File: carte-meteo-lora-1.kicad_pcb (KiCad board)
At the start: 2 copper layers, 60 x 45 mm, 121 parts, among them J1 TC2030, J2 Conn_01x04, J3 Conn_01x04, J4 Conn_Coaxial, J5 USB_C_Receptacle_USB2.0_14P, J6 Solar_Cell, J7 Conn_01x02, J8 Battery_Cell, Q1 AO4882, Q2 AO4882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

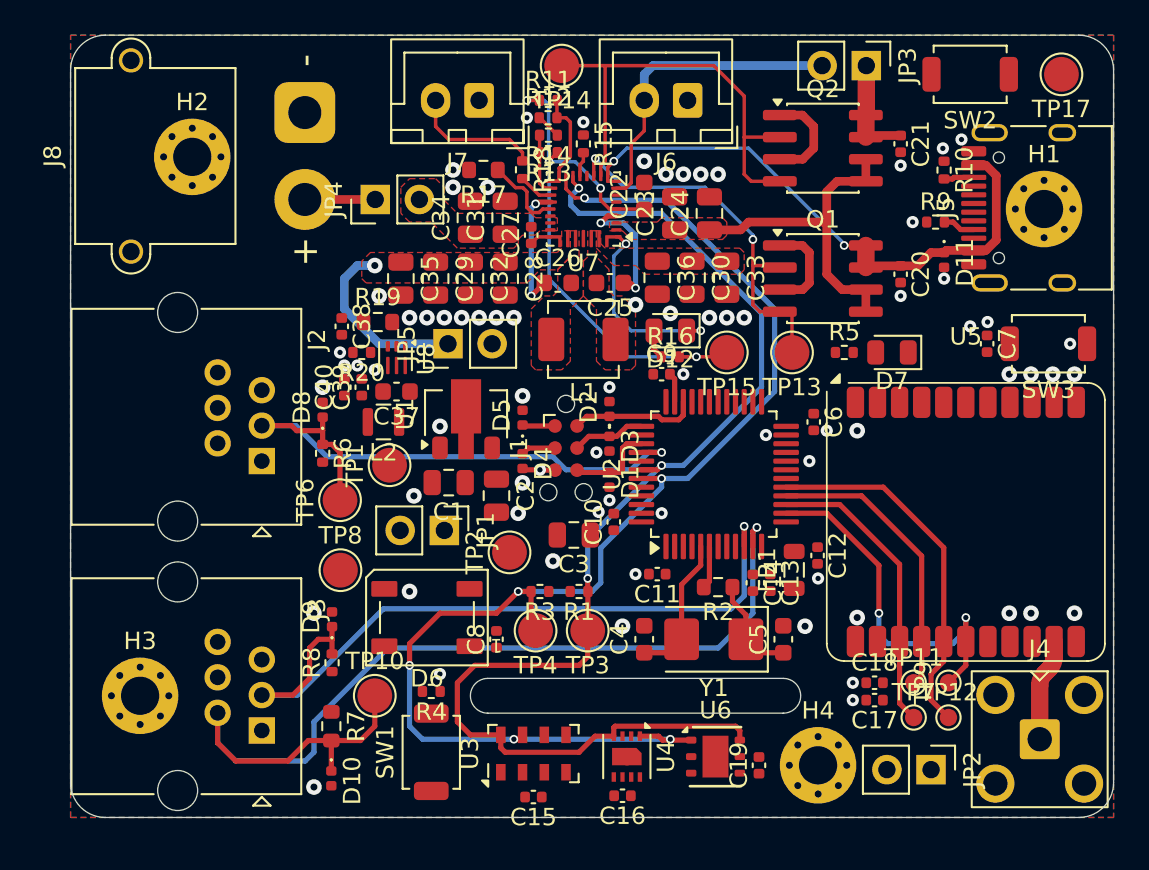
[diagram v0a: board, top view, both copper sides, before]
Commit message: pcb: add smps and +5v pwr routing
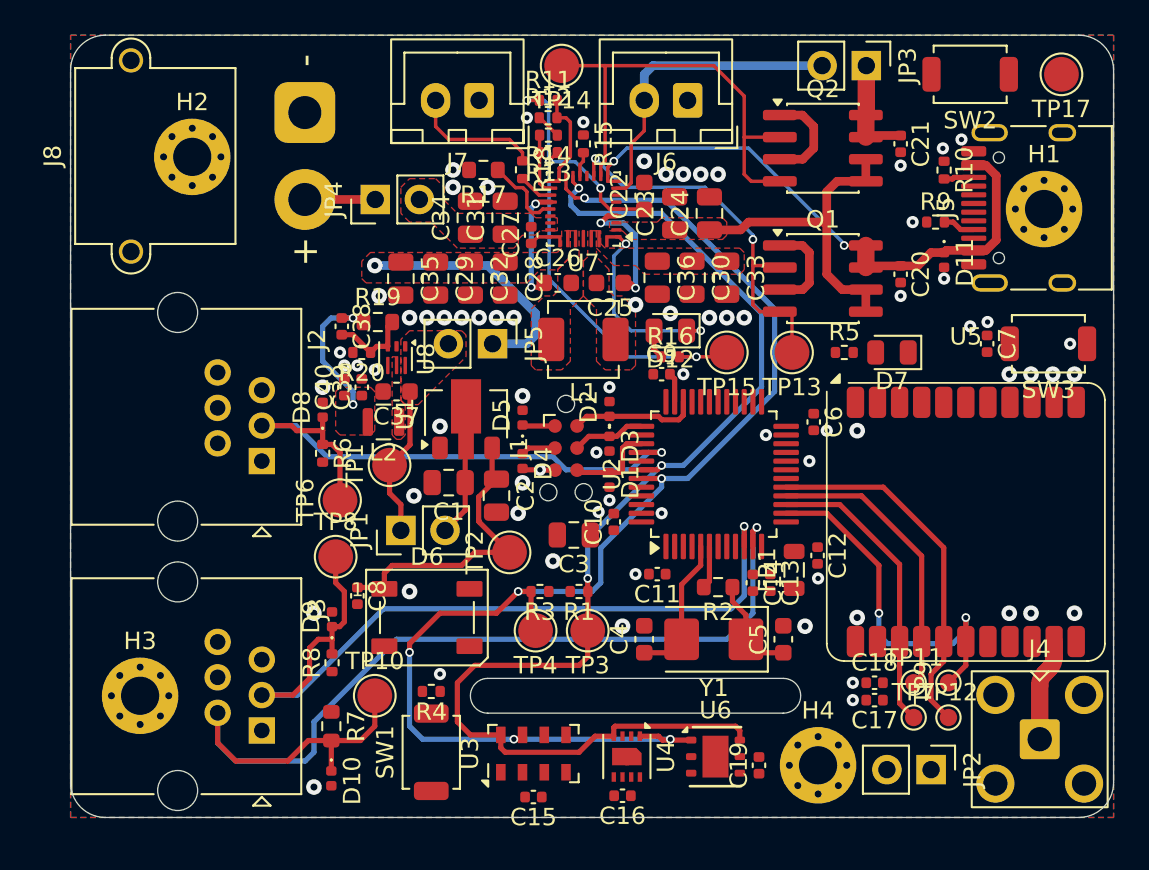
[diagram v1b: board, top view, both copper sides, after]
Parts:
- moved C8 8.38 mm to (66.5, 55.2), turned to -90 degrees
- moved JP5 2.57 mm to (74.3, 40.8), turned to -90 degrees
- moved JP1 2.50 mm to (69.0, 51.5), turned to 90 degrees
- moved TP8 0.82 mm to (65.2, 53.0)
- turned D6 to 0 degrees
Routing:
- net +SYS: track 10.6 -> 28.4 mm
- net +5V: track 0.00 -> 17.5 mm
- net +3V3: track 1.89 -> 10.4 mm, vias 0 -> 2
- net /WIND: track 43.2 -> 48.0 mm
- net Net-(U8-FB): track 0.00 -> 4.72 mm
- net Net-(U7-BTST2): track 7.39 -> 6.69 mm
- added copper zone on F.Cu, net +3V3
- added copper zone on F.Cu, net Net-(U8-SW)

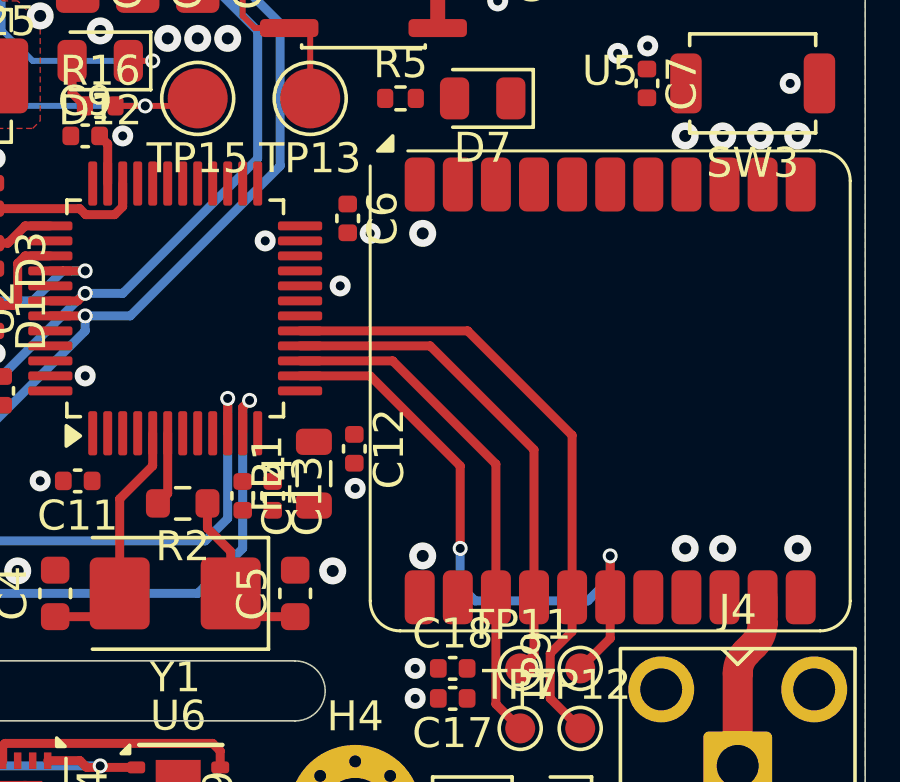
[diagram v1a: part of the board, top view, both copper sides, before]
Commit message: pcb: add lora gpio routing
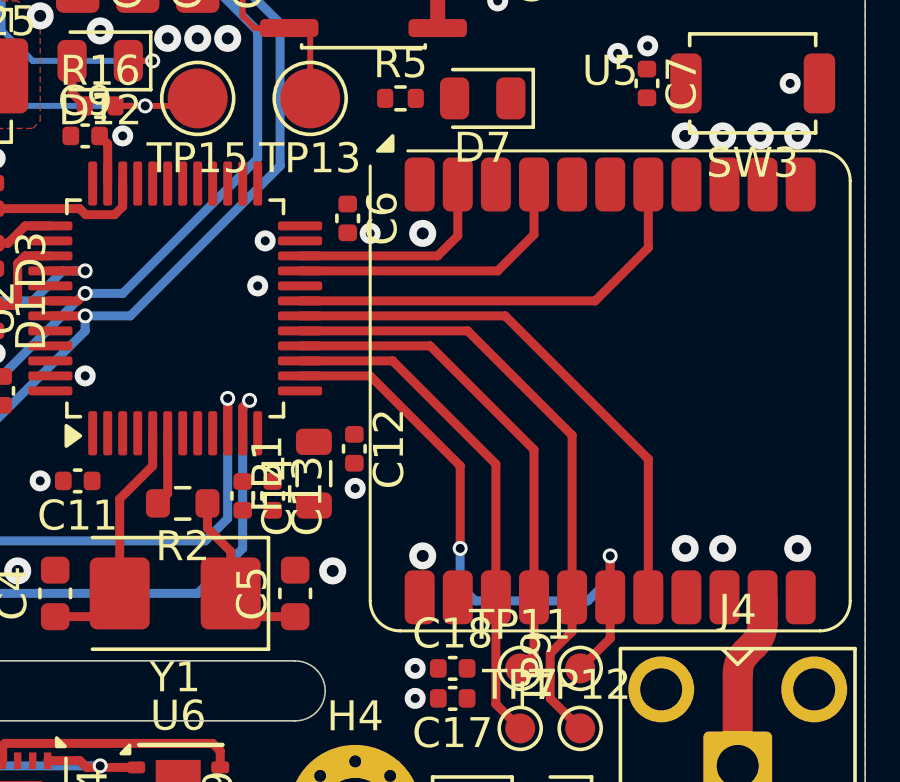
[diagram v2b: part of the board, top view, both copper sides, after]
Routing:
- net /RST: track 0.00 -> 18.2 mm
- net /DIO1: track 0.00 -> 14.5 mm
- net /DIO3: track 0.00 -> 9.97 mm
- net /BUSY: track 0.00 -> 7.25 mm
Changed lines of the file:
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@@
 	)
 	(via
-		(at 92.5 47.5)
+		(at 89.75 47.5)
 		(size 0.7)
 		(drill 0.3)
@@
 	)
 	(segment
+		(start 98 48.5)
+		(end 102.77 53.27)
+		(width 0.3)
+		(layer "F.Cu")
+		(net "/RST")
+	)
+	(segment
+		(start 91.1625 48.5)
+		(end 98 48.5)
+		(width 0.3)
+		(layer "F.Cu")
+		(net "/RST")
+	)
+	(segment
+		(start 102.77 53.27)
+		(end 102.77 57.88)
+		(width 0.3)
+		(layer "F.Cu")
+		(net "/RST")
+	)
+	(segment
+		(start 98.96 45.79)
+		(end 98.96 44.12)
+		(width 0.3)
+		(layer "F.Cu")
+		(net "/DIO3")
+	)
+	(segment
+		(start 97.75 47)
+		(end 98.96 45.79)
+		(width 0.3)
+		(layer "F.Cu")
+		(net "/DIO3")
+	)
+	(segment
+		(start 91.1625 47)
+		(end 97.75 47)
+		(width 0.3)
+		(layer "F.Cu")
+		(net "/DIO3")
+	)
+	(segment
+		(start 101 48)
+		(end 102.77 46.23)
+		(width 0.3)
+		(layer "F.Cu")
+		(net "/DIO1")
+	)
+	(segment
+		(start 91.1625 48)
+		(end 101 48)
+		(width 0.3)
+		(layer "F.Cu")
+		(net "/DIO1")
+	)
+	(segment
+		(start 102.77 46.23)
+		(end 102.77 44.12)
+		(width 0.3)
+		(layer "F.Cu")
+		(net "/DIO1")
+	)
+	(segment
+		(start 91.1625 46.5)
+		(end 95.75 46.5)
+		(width 0.3)
+		(layer "F.Cu")
+		(net "/BUSY")
+	)
+	(segment
+		(start 96.42 45.83)
+		(end 96.42 44.12)
+		(width 0.3)
+		(layer "F.Cu")
+		(net "/BUSY")
+	)
+	(segment
+		(start 95.75 46.5)
+		(end 96.42 45.83)
+		(width 0.3)
+		(layer "F.Cu")
+		(net "/BUSY")
+	)
+	(segment

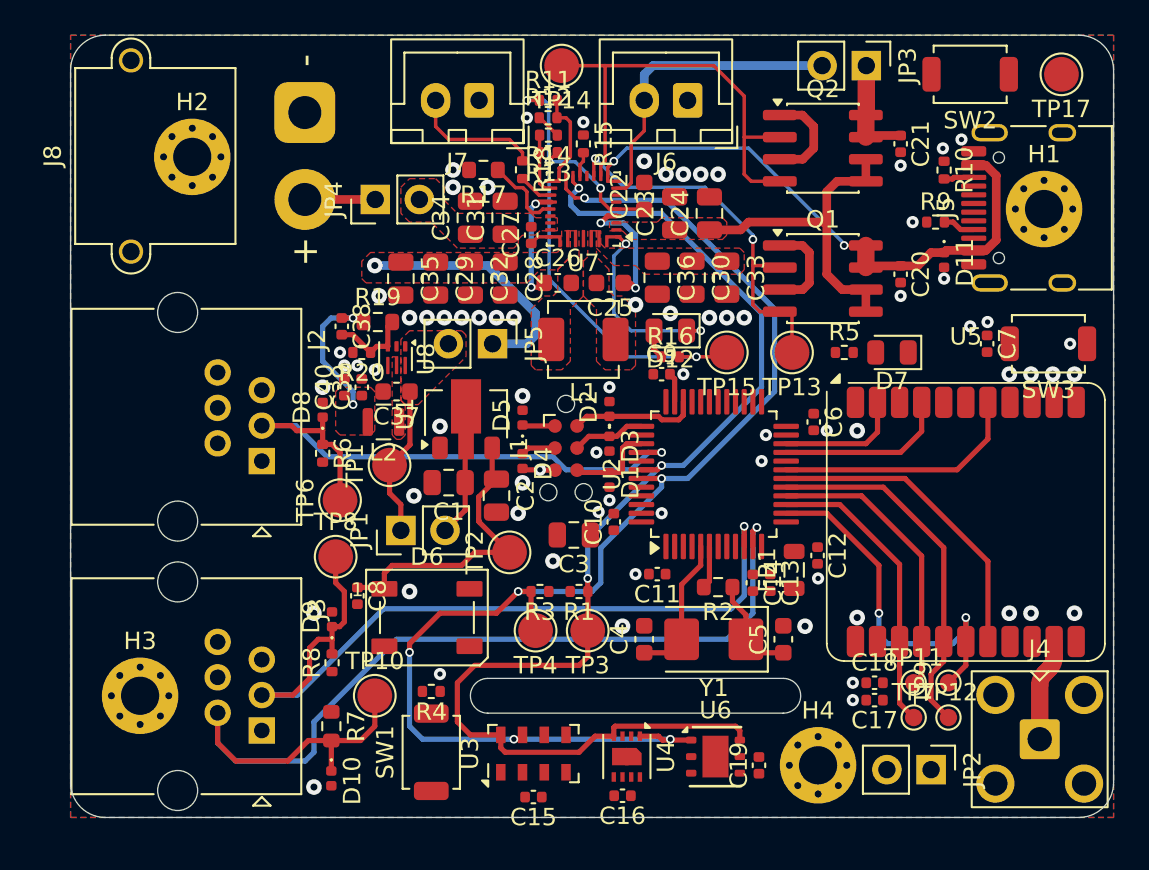
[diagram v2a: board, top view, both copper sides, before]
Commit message: pcb: add boot/rst routing
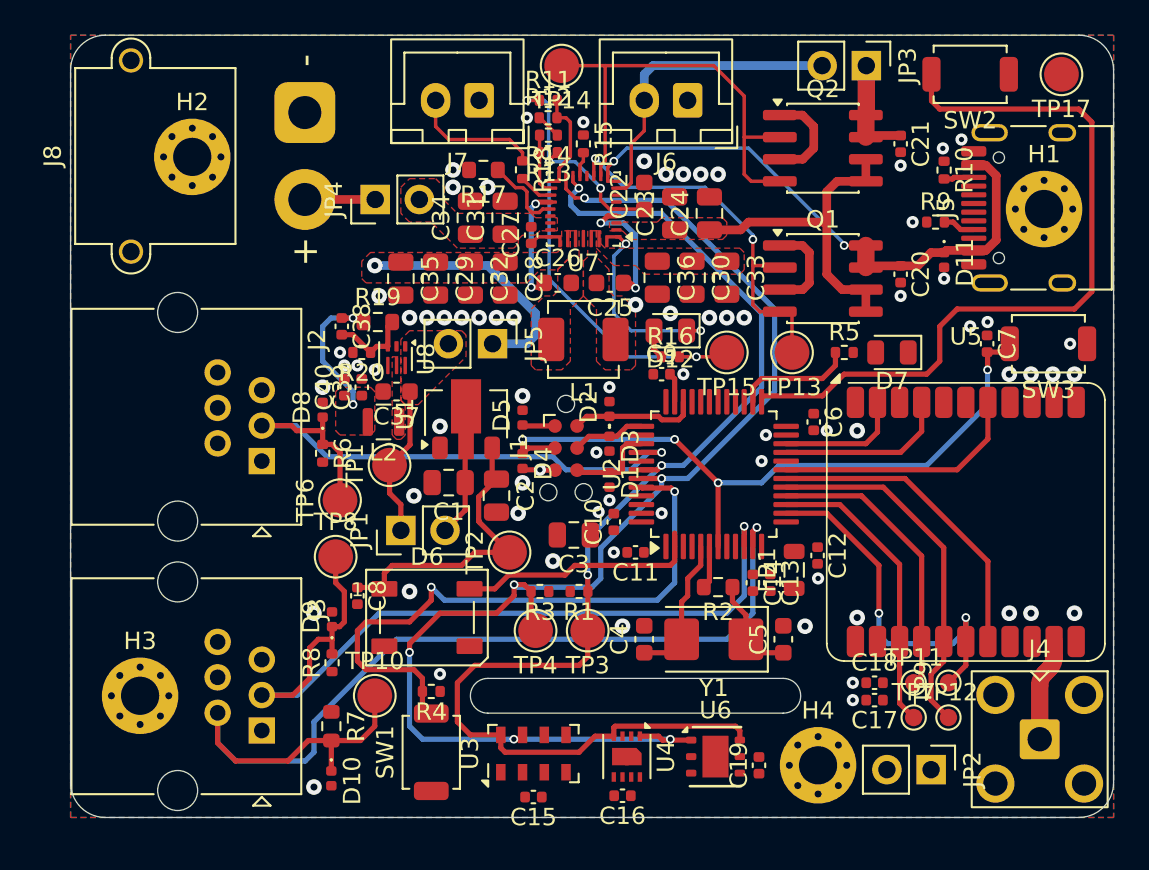
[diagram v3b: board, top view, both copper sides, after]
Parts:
- moved C11 1.77 mm to (82.5, 52.8)
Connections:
- R5 pad 1: Net-(U2-PB12) -> Net-(U2-PB13)
- U2 pad 25: Net-(U2-PB12) -> /BTN1
- U2 pad 26: /BTN1 -> Net-(U2-PB13)
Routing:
- net /BTN1: track 0.00 -> 44.0 mm
- net /NRST: track 2.00 -> 40.7 mm, vias 0 -> 4
- net /BOOT: track 0.00 -> 35.9 mm, vias 0 -> 2
- net /RGB1: track 0.00 -> 14.1 mm
- net Net-(U2-PB13): track 0.00 -> 6.86 mm
- net /SDA: track 76.8 -> 77.5 mm

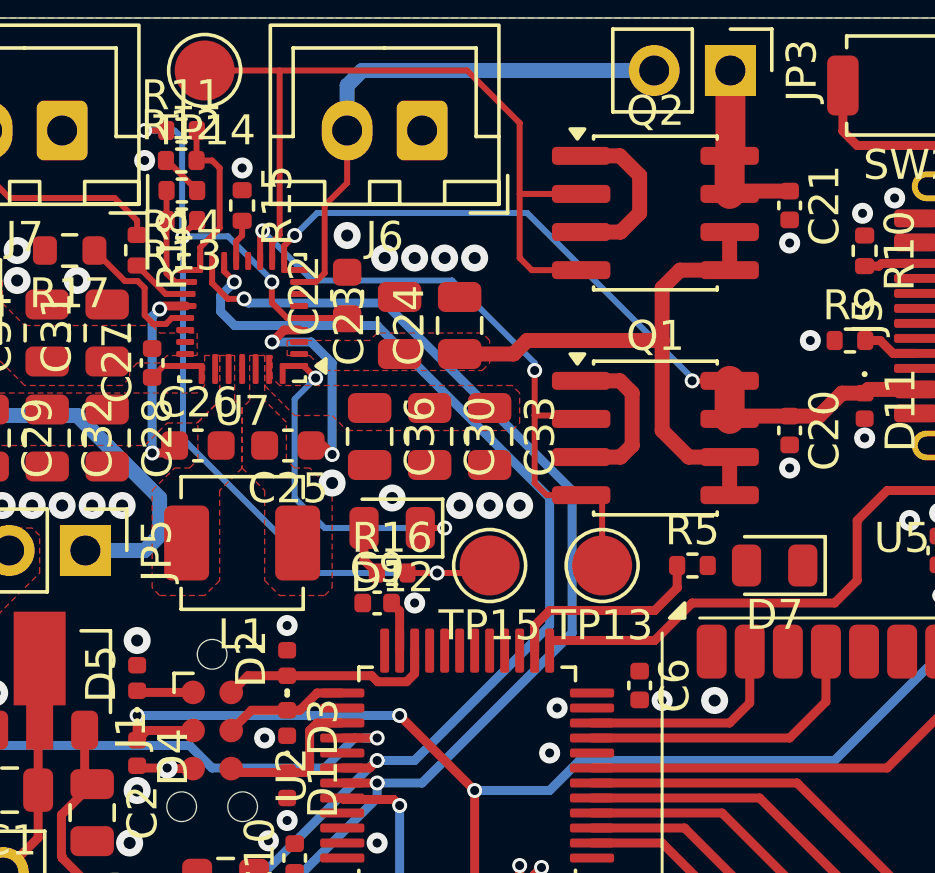
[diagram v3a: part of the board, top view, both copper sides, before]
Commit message: pcb: connect charger to mcu
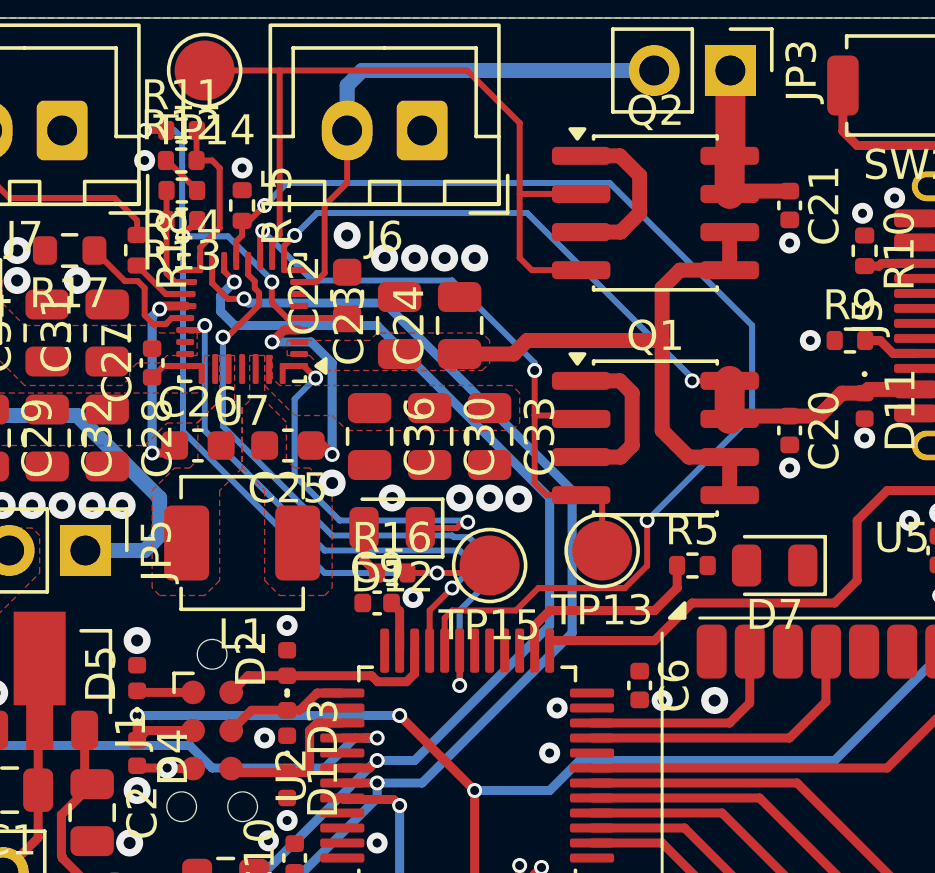
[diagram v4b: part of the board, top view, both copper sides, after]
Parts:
- moved TP13 0.50 mm to (91.5, 40.8)
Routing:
- net /Power/~{CE}: track 1.42 -> 38.9 mm, vias 0 -> 2
- net /Power/~{QON}: track 0.00 -> 22.6 mm, vias 0 -> 2
- net /Power/~{INT}: track 0.00 -> 18.3 mm, vias 0 -> 2
- net Net-(D12-K): track 11.2 -> 12.3 mm

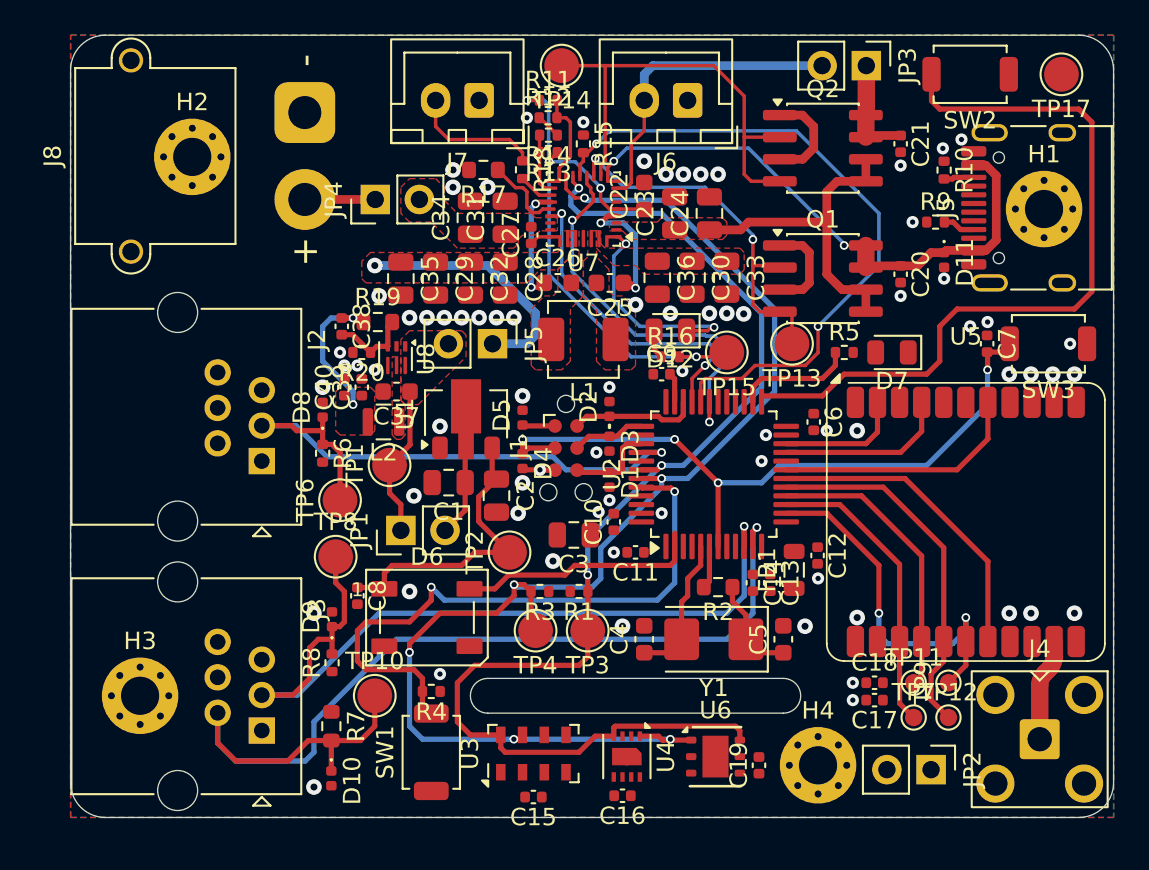
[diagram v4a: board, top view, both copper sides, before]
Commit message: pcb: add +3v3 pwr routing
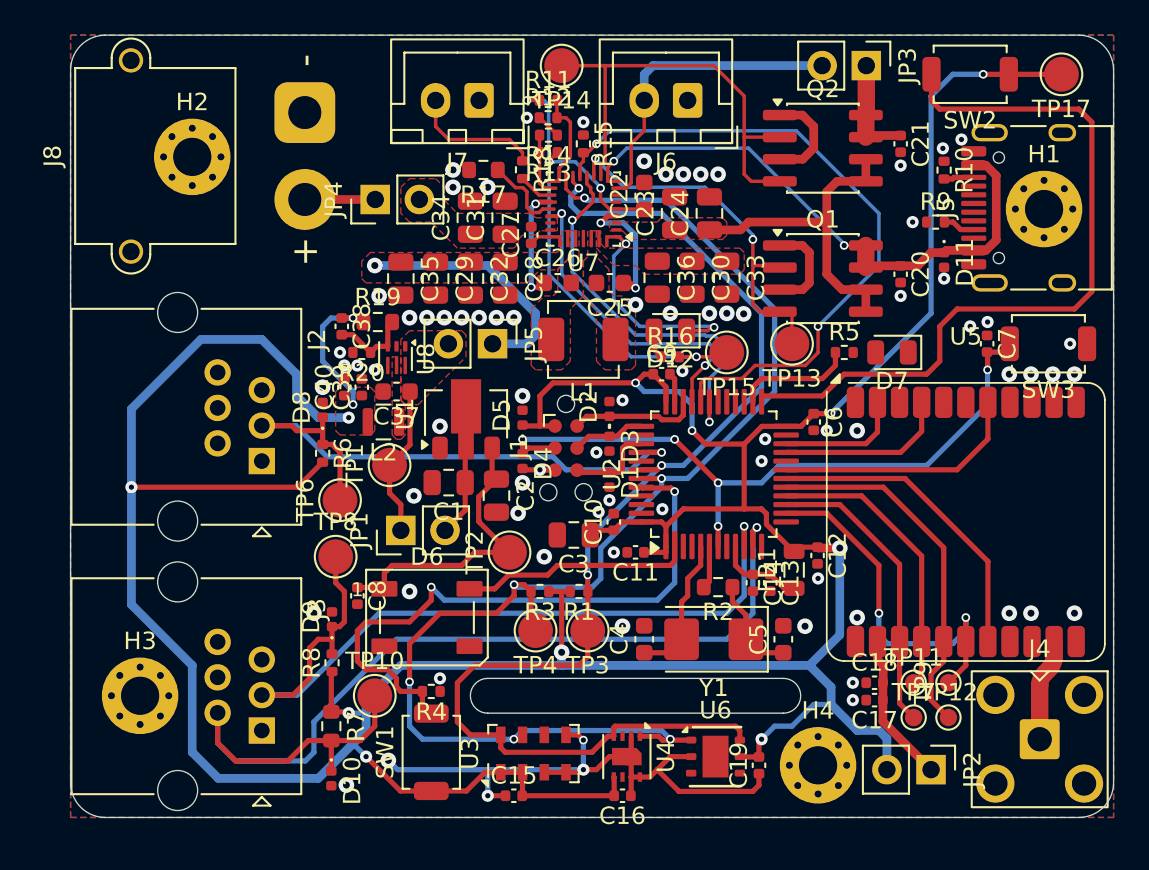
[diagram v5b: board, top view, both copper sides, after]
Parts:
- moved C15 1.13 mm to (75.5, 66.8), turned to 0 degrees
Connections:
- U2 pad 12: /ALERT -> unconnected-(U2-PA2-Pad12)
- U4 pad 3: /ALERT -> unconnected-(U4-ALERT-Pad3)
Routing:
- net +3V3: track 10.4 -> 237.5 mm, vias 2 -> 13
- net GND: track 5.06 -> 41.7 mm, vias 72 -> 76
- net Net-(U2-VDDA): track 0.00 -> 5.01 mm
- net /NRST: vias 4 -> 5
